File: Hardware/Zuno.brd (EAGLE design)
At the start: 160 x 100 mm, 7 parts, among them Q1 2N3904, X1 5566-24

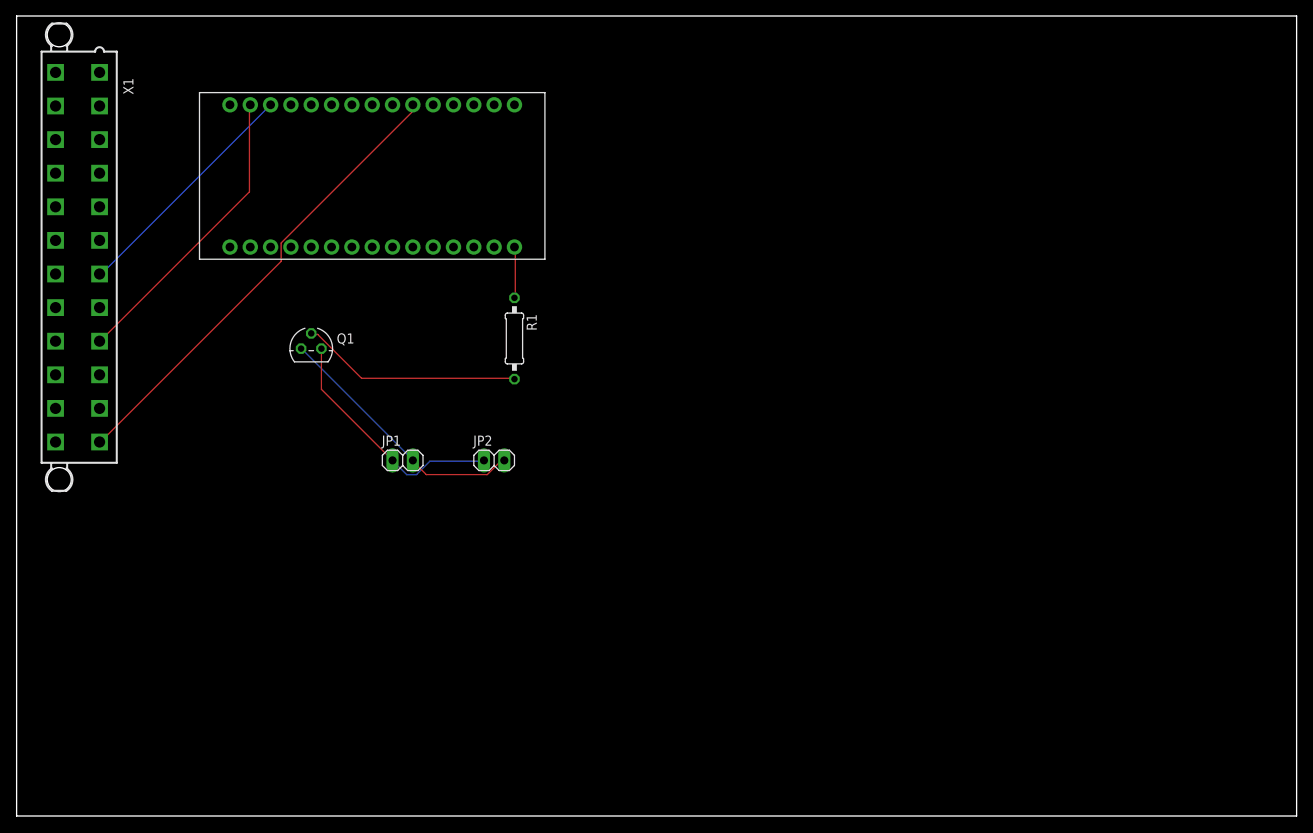
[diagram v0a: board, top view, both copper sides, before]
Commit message: Updated board to include drill holes
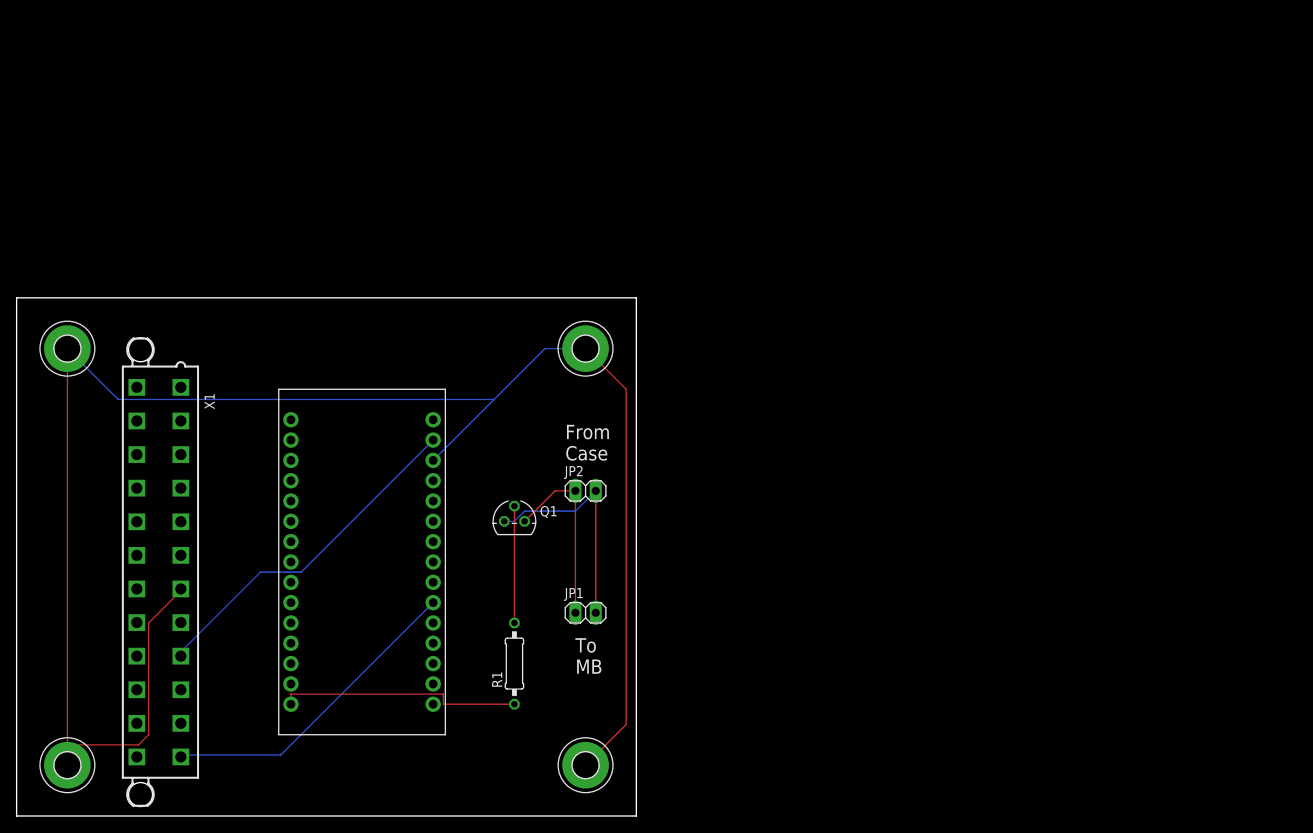
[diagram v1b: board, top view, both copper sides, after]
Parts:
- removed FRAME1: FRAME-LETTER, SparkFun-Aesthetics:CREATIVE_COMMONS
- added H1, H2, H3, H4: MOUNT-PAD-ROUND3.2, holes:3,2-PAD
- moved U$1 52.1 mm to (44.5, 29.2), turned to 270 degrees
- moved X1 40.7 mm to (17.8, 30.5)
- moved R1 40.6 mm to (62.2, 19.1), turned to 90 degrees
- moved Q1 33.3 mm to (62.2, 36.8)
- moved JP1 29.8 mm to (71.1, 25.4)
- moved JP2 12.0 mm to (71.1, 40.6)
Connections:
- net N$1 renamed VCC
- removed net N$2: U$1.P$3, X1.7
- new net GND: H1.B3,2, H2.B3,2, H3.B3,2, H4.B3,2, U$1.P$3, X1.7
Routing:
- net GND: track 0.00 -> 219.7 mm
- net N$2: track 30.2 -> 0.00 mm
- net N$4: track 6.49 -> 30.5 mm
- net N$3: track 58.4 -> 40.0 mm
- net N$5: track 27.8 -> 14.6 mm
- net TOMOTHERBOARD: track 30.6 -> 23.2 mm
- net VCC: track 37.4 -> 43.2 mm
- net N$7: track 32.8 -> 28.2 mm
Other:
- board size 160 x 100 mm -> 77.5 x 64.8 mm
- board text added: "From Case"
- board text added: "To MB"
